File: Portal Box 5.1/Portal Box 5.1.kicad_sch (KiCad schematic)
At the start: 80 parts, among them J1 USB_A, J2 USB_C, J3 A 14-LC-TT, J4 6871XX149022_687118149022, J5 RFID-RC522, J6 Conn_01x04, K1 PR28-5V-360-1A-E, K2 DIP05-2A72-21L, Q1 NTR5103NT1G, Q2 NTR5103NT1G, SW1 BUTTON, SW2 SW_DPST, U1 USBLC6-2P6, U2 USBLC6-2P6, U3 TLE4971-A050T5-U-E0001, U4 AP7363-33D-13, U5 ESP32-S3-DEVKITC-1-N8R8-OFFIC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

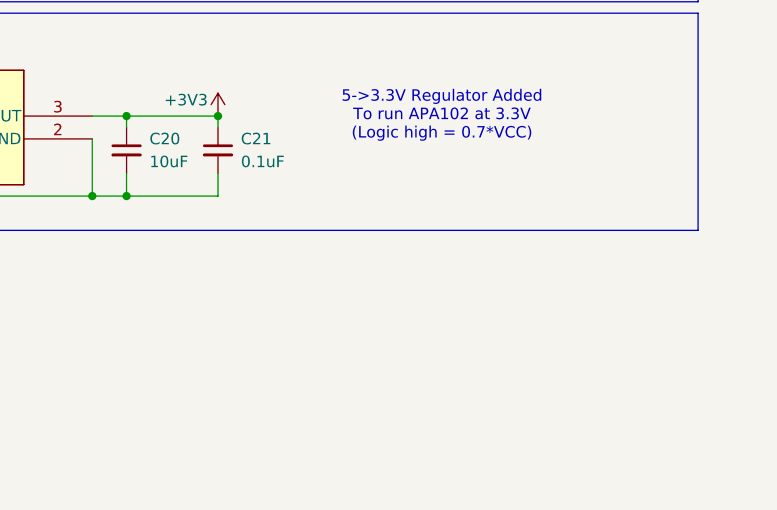
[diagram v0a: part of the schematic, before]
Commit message: update track clearances, mfg files
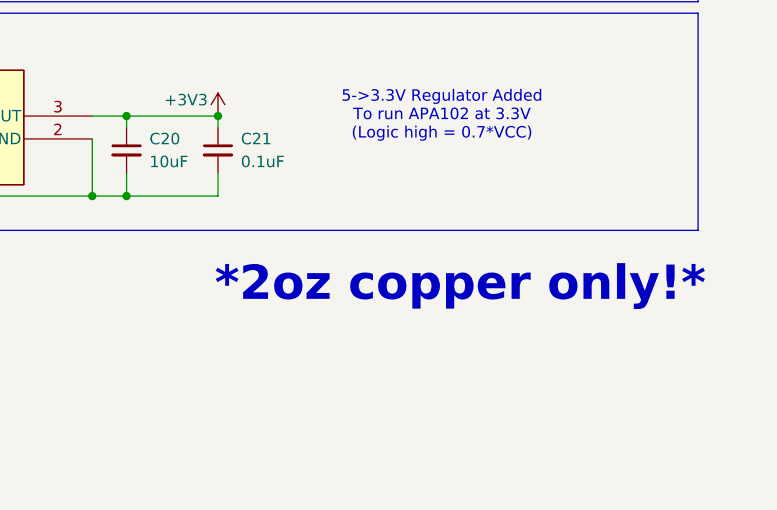
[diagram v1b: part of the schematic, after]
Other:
- note added: "*2oz copper only!*"
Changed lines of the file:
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@@
+		)
+	)
+	(text "*2oz copper only!*"
+		(exclude_from_sim no)
+		(at 269.494 220.726 0)
+		(effects
+			(font
+				(size 3.81 3.81)
+				(thickness 1.27)
+				(bold yes)
+				(color 255 0 0 1)
+			)
 		)
 	)

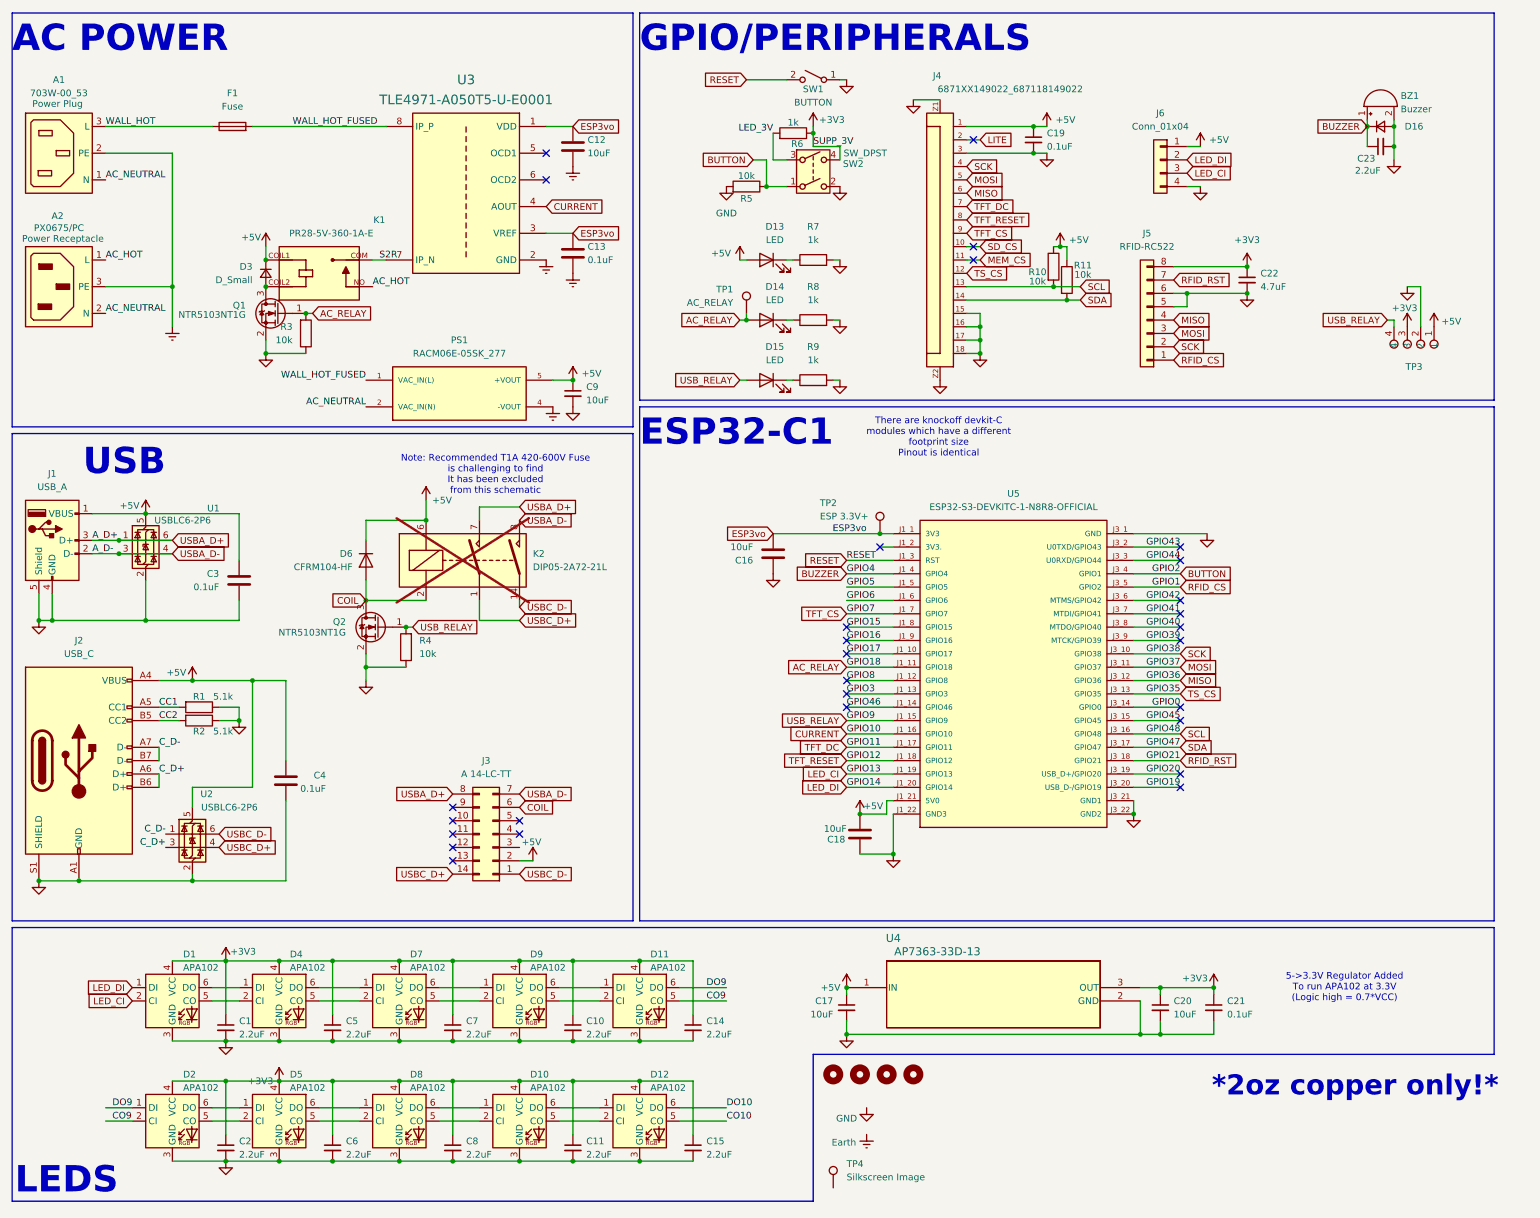
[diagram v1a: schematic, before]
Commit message: changed some part numbers, update csv
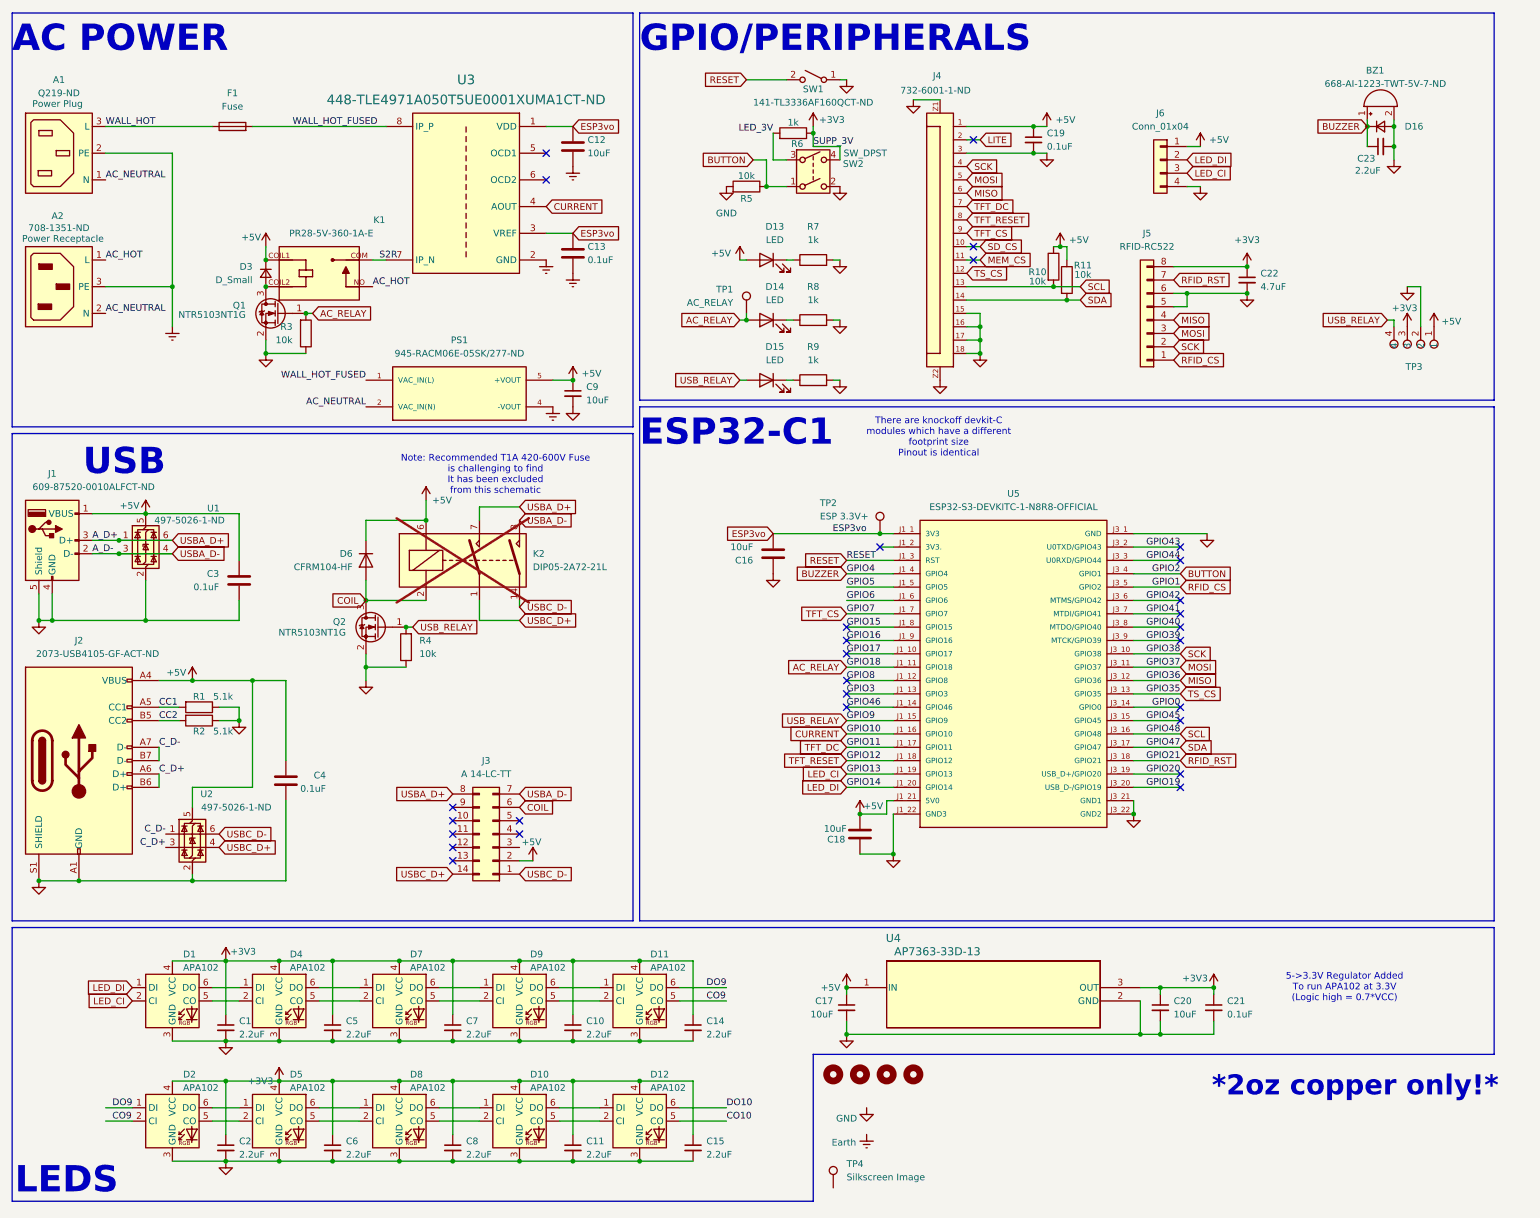
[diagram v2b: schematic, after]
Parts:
- A1: value 703W-00_53 -> Q219-ND
- A2: value PX0675/PC -> 708-1351-ND
- BZ1: value Buzzer -> 668-AI-1223-TWT-5V-7-ND
- J1: value USB_A -> 609-87520-0010ALFCT-ND
- J2: value USB_C -> 2073-USB4105-GF-ACT-ND
- J4: value 6871XX149022_687118149022 -> 732-6001-1-ND
- PS1: value RACM06E-05SK_277 -> 945-RACM06E-05SK/277-ND
- SW1: value BUTTON -> 141-TL3336AF160QCT-ND
- U1, U2: value USBLC6-2P6 -> 497-5026-1-ND
- U3: value TLE4971-A050T5-U-E0001 -> 448-TLE4971A050T5UE0001XUMA1CT-ND
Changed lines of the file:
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@@
 			)
 		)
-		(property "Value" "PX0675/PC"
+		(property "Value" "708-1351-ND"
 			(at 22.86 57.404 0)
 			(effects
@@
 			)
 		)
-		(property "Value" "BUTTON"
+		(property "Value" "141-TL3336AF160QCT-ND"
 			(at 166.37 33.528 0)
 			(effects
@@
 		(on_board yes)
 		(dnp no)
-		(fields_autoplaced yes)
 		(property "Reference" "J2"
 			(at 26.67 135.89 0)
@@
 			)
 		)
-		(property "Value" "USB_C"
-			(at 26.67 138.43 0)
+		(property "Value" "2073-USB4105-GF-ACT-ND"
+			(at 30.226 138.43 0)
 			(effects
 				(font
@@
 			)
 		)
-		(property "Value" "USBLC6-2P6"
+		(property "Value" "497-5026-1-ND"
 			(at 49.9111 167.64 0)
 			(effects
@@
 			)
 		)
-		(property "Value" "USBLC6-2P6"
+		(property "Value" "497-5026-1-ND"
 			(at 41.0211 113.03 0)
 			(effects
@@
 			)
 		)
-		(property "Value" "703W-00_53"
+		(property "Value" "Q219-ND"
 			(at 22.86 31.75 0)
 			(effects
@@
 			)
 		)
-		(property "Value" "TLE4971-A050T5-U-E0001"
+		(property "Value" "448-TLE4971A050T5UE0001XUMA1CT-ND"
 			(at 100.33 33.02 0)
 			(effects
@@
 			)
 		)
-		(property "Value" "RACM06E-05SK_277"
+		(property "Value" "945-RACM06E-05SK/277-ND"
 			(at 99.06 81.28 0)
 			(effects
@@
 			)
 		)
-		(property "Value" "6871XX149022_687118149022"
-			(at 217.678 30.988 90)
+		(property "Value" "732-6001-1-ND"
+			(at 196.342 31.242 90)
 			(effects
 				(font
@@
 		(on_board yes)
 		(dnp no)
-		(fields_autoplaced yes)
 		(property "Reference" "BZ1"
-			(at 278.13 32.2648 90)
+			(at 271.526 27.432 90)
 			(effects
 				(font
@@
 			)
 		)
-		(property "Value" "Buzzer"
-			(at 278.13 34.8048 90)
+		(property "Value" "668-AI-1223-TWT-5V-7-ND"
+			(at 263.652 29.972 90)
 			(effects
 				(font
@@
 		(on_board yes)
 		(dnp no)
-		(fields_autoplaced yes)
 		(property "Reference" "J1"
 			(at 21.59 104.14 0)
@@
 			)
 		)
-		(property "Value" "USB_A"
-			(at 21.59 106.68 0)
+		(property "Value" "609-87520-0010ALFCT-ND"
+			(at 29.464 106.68 0)
 			(effects
 				(font

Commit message: update to 5.1.1
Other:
- note added: "Should these be Earth or DC ground?"
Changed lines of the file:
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@@
 		(title "PortalBox Project")
 		(date "2025-10-25")
-		(rev "V5.06")
+		(rev "V5.1.1")
 		(company "Bucknell University | Electrical and Computer Engineering ")
 		(comment 1 "Aiden Cherniske & Elisha Foster")
@@
 		)
 	)
+	(text "Should these be Earth or DC ground?"
+		(exclude_from_sim no)
+		(at 112.776 70.358 0)
+		(effects
+			(font
+				(size 1.27 1.27)
+			)
+		)
+	)

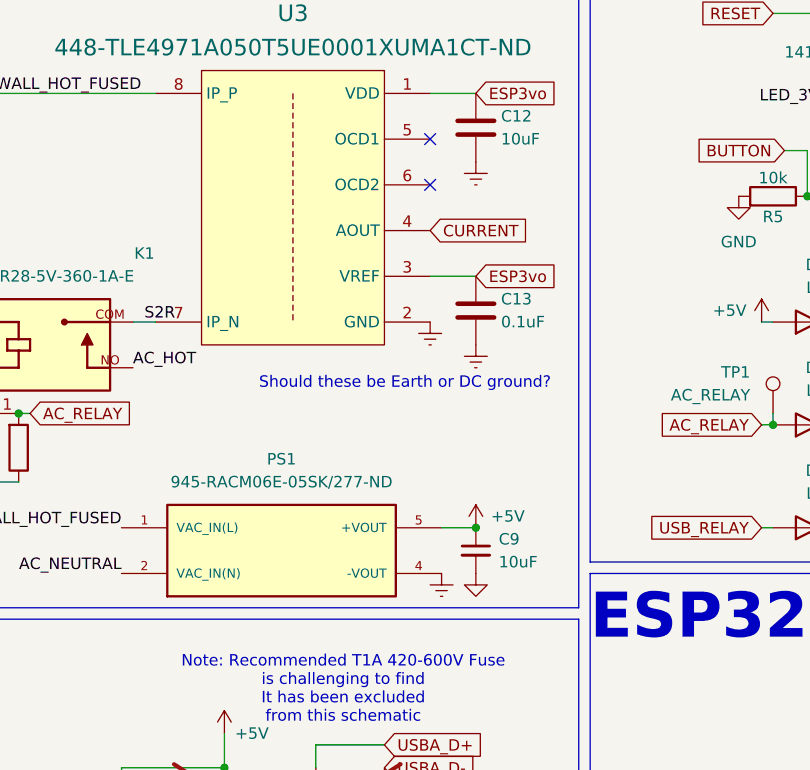
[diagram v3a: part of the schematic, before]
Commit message: change ac/dc and acm to dc ground, update planes
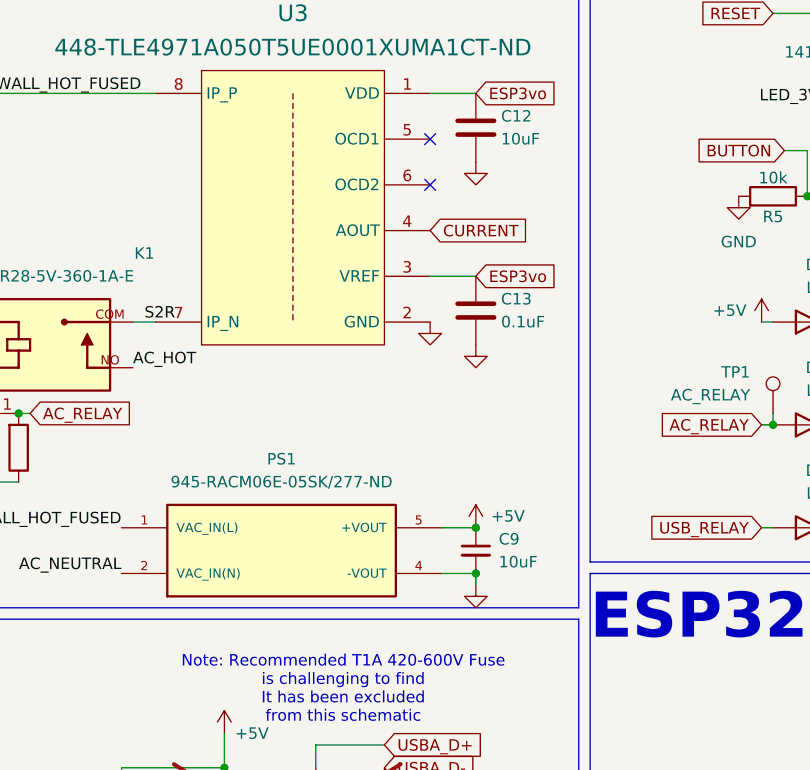
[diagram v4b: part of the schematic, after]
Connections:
- net Earth: no longer C12.2, C13.2, PS1.4 (-VOUT), U3.2 (GND)
- net GND: now also C12.2, C13.2, PS1.4 (-VOUT), U3.2 (GND)
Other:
- note removed: "Should these be Earth or DC ground?"

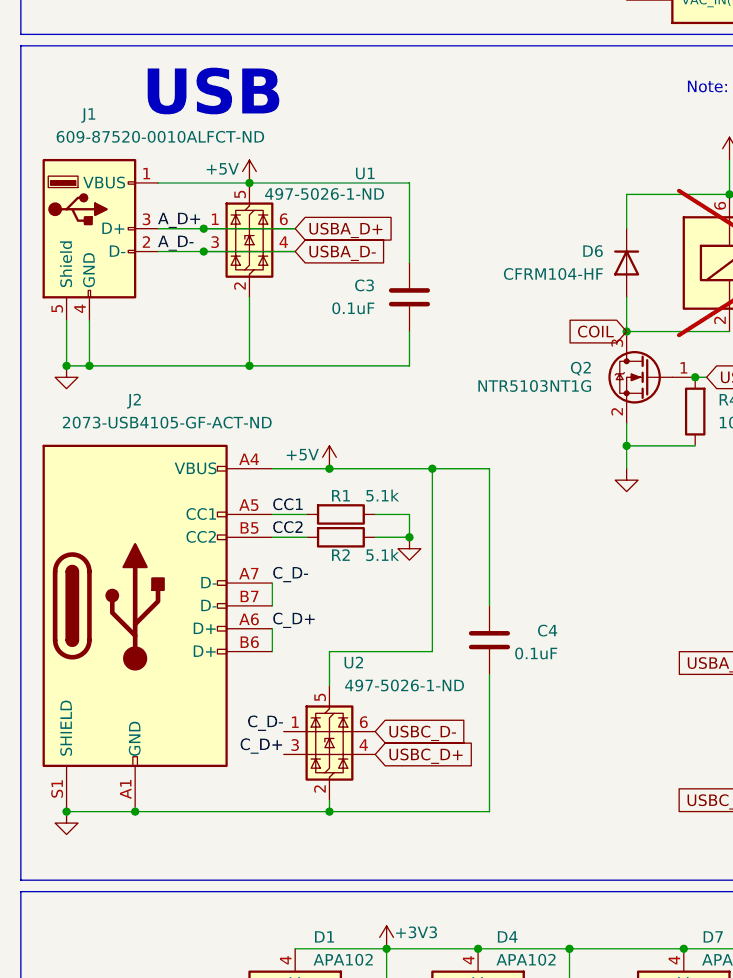
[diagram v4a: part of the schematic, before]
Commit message: fix ground plane bulges, schematic and layout change for TVS diodes
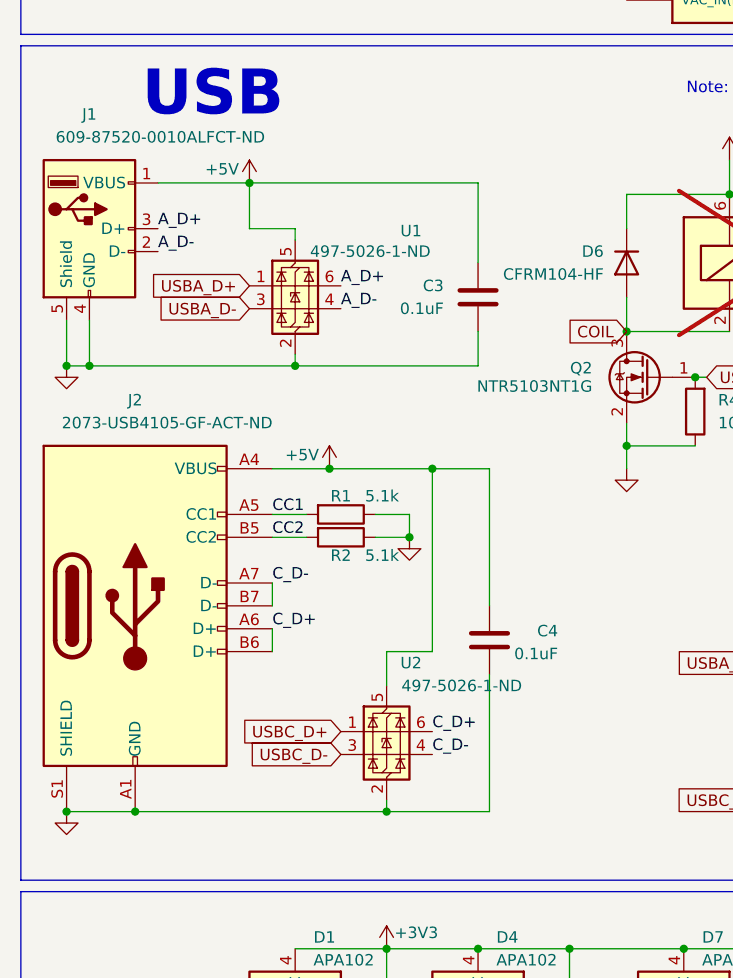
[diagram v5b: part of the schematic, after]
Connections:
- net C_D+: now also U2.6 (I/O1); no longer U2.3 (I/O2)
- net C_D-: now also U2.4 (I/O2); no longer U2.1 (I/O1)
- net USBA_D+: no longer J1.3 (D+), U1.6 (I/O1)
- net USBA_D-: no longer J1.2 (D-), U1.4 (I/O2)
- net USBC_D+: now also U2.1 (I/O1); no longer U2.4 (I/O2)
- net USBC_D-: now also U2.3 (I/O2); no longer U2.6 (I/O1)
- new net A_D+: J1.3 (D+), U1.6 (I/O1)
- new net A_D-: J1.2 (D-), U1.4 (I/O2)
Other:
- moved on the sheet: C3, U1, U2
